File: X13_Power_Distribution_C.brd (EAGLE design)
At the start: 152.4 x 73.7 mm, 34 parts, among them Q1 IRF1018EPBF, Q2 310mA/60V/1.6Ω, Q3 IRF1018EPBF, Q4 IRF1018EPBF

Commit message: Version C! Uses connector C!
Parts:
- removed BRICK1, BRICK2: DIST2BRICK_B, Brick_Dist_Connector:DIST2BRICK_B
- added BRICK_A, BRICK_B: DIST2BRICK_C, Brick_Dist_Connector:DIST2BRICK_C
- moved R7 1.27 mm to (85.1, 24.1)
- moved R4 1.27 mm to (77.5, 24.1)
- moved R6 1.27 mm to (81.3, 24.1)
- moved R8 1.27 mm to (73.7, 24.1)
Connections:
- net +12V_A: now also BRICK_A.2@1, BRICK_A.2@10, BRICK_A.2@11, BRICK_A.2@12, BRICK_A.2@13, BRICK_A.2@14, BRICK_A.2@15, BRICK_A.2@16, BRICK_A.2@2, BRICK_A.2@3, BRICK_A.2@4, BRICK_A.2@5, BRICK_A.2@6, BRICK_A.2@7, BRICK_A.2@8, BRICK_A.2@9; no longer BRICK1.2@1, BRICK1.2@10, BRICK1.2@11, BRICK1.2@12, BRICK1.2@13, BRICK1.2@14, BRICK1.2@15, BRICK1.2@16, BRICK1.2@2, BRICK1.2@3, BRICK1.2@4, BRICK1.2@5, BRICK1.2@6, BRICK1.2@7, BRICK1.2@8, BRICK1.2@9
- net +12V_B: now also BRICK_B.2@1, BRICK_B.2@10, BRICK_B.2@11, BRICK_B.2@12, BRICK_B.2@13, BRICK_B.2@14, BRICK_B.2@15, BRICK_B.2@16, BRICK_B.2@2, BRICK_B.2@3, BRICK_B.2@4, BRICK_B.2@5, BRICK_B.2@6, BRICK_B.2@7, BRICK_B.2@8, BRICK_B.2@9; no longer BRICK2.2@1, BRICK2.2@10, BRICK2.2@11, BRICK2.2@12, BRICK2.2@13, BRICK2.2@14, BRICK2.2@15, BRICK2.2@16, BRICK2.2@2, BRICK2.2@3, BRICK2.2@4, BRICK2.2@5, BRICK2.2@6, BRICK2.2@7, BRICK2.2@8, BRICK2.2@9
- net +48V: now also BRICK_A.1@1, BRICK_A.1@10, BRICK_A.1@2, BRICK_A.1@3, BRICK_A.1@4, BRICK_A.1@5, BRICK_A.1@6, BRICK_A.1@7, BRICK_A.1@8, BRICK_A.1@9, BRICK_B.1@1, BRICK_B.1@10, BRICK_B.1@2, BRICK_B.1@3, BRICK_B.1@4, BRICK_B.1@5, BRICK_B.1@6, BRICK_B.1@7, BRICK_B.1@8, BRICK_B.1@9; no longer BRICK1.1@1, BRICK1.1@10, BRICK1.1@2, BRICK1.1@3, BRICK1.1@4, BRICK1.1@5, BRICK1.1@6, BRICK1.1@7, BRICK1.1@8, BRICK1.1@9, BRICK2.1@1, BRICK2.1@10, BRICK2.1@2, BRICK2.1@3, BRICK2.1@4, BRICK2.1@5, BRICK2.1@6, BRICK2.1@7, BRICK2.1@8, BRICK2.1@9
- net 12V_GND: now also BRICK_A.4@1, BRICK_A.4@10, BRICK_A.4@11, BRICK_A.4@12, BRICK_A.4@13, BRICK_A.4@14, BRICK_A.4@15, BRICK_A.4@16, BRICK_A.4@2, BRICK_A.4@3, BRICK_A.4@4, BRICK_A.4@5, BRICK_A.4@6, BRICK_A.4@7, BRICK_A.4@8, BRICK_A.4@9, BRICK_B.4@1, BRICK_B.4@10, BRICK_B.4@11, BRICK_B.4@12, BRICK_B.4@13, BRICK_B.4@14, BRICK_B.4@15, BRICK_B.4@16, BRICK_B.4@2, BRICK_B.4@3, BRICK_B.4@4, BRICK_B.4@5, BRICK_B.4@6, BRICK_B.4@7, BRICK_B.4@8, BRICK_B.4@9; no longer BRICK1.4@1, BRICK1.4@10, BRICK1.4@11, BRICK1.4@12, BRICK1.4@13, BRICK1.4@14, BRICK1.4@15, BRICK1.4@16, BRICK1.4@2, BRICK1.4@3, BRICK1.4@4, BRICK1.4@5, BRICK1.4@6, BRICK1.4@7, BRICK1.4@8, BRICK1.4@9, BRICK2.4@1, BRICK2.4@10, BRICK2.4@11, BRICK2.4@12, BRICK2.4@13, BRICK2.4@14, BRICK2.4@15, BRICK2.4@16, BRICK2.4@2, BRICK2.4@3, BRICK2.4@4, BRICK2.4@5, BRICK2.4@6, BRICK2.4@7, BRICK2.4@8, BRICK2.4@9
- net 48V_GND: now also BRICK_A.3@1, BRICK_A.3@10, BRICK_A.3@2, BRICK_A.3@3, BRICK_A.3@4, BRICK_A.3@5, BRICK_A.3@6, BRICK_A.3@7, BRICK_A.3@8, BRICK_A.3@9, BRICK_B.3@1, BRICK_B.3@10, BRICK_B.3@2, BRICK_B.3@3, BRICK_B.3@4, BRICK_B.3@5, BRICK_B.3@6, BRICK_B.3@7, BRICK_B.3@8, BRICK_B.3@9; no longer BRICK1.3@1, BRICK1.3@10, BRICK1.3@2, BRICK1.3@3, BRICK1.3@4, BRICK1.3@5, BRICK1.3@6, BRICK1.3@7, BRICK1.3@8, BRICK1.3@9, BRICK2.3@1, BRICK2.3@10, BRICK2.3@2, BRICK2.3@3, BRICK2.3@4, BRICK2.3@5, BRICK2.3@6, BRICK2.3@7, BRICK2.3@8, BRICK2.3@9
- net ALERT_1: now also BRICK_A.D; no longer BRICK1.D
- net ALERT_2: now also BRICK_B.D; no longer BRICK2.D
- net C2_1: now also BRICK_A.A; no longer BRICK1.A
- net C2_2: now also BRICK_B.A; no longer BRICK2.A
- net CLK: now also BRICK_A.C, BRICK_B.C; no longer BRICK1.C, BRICK2.C
- net DATA: now also BRICK_A.E, BRICK_B.E; no longer BRICK1.E, BRICK2.E
- net ON/OFF: now also BRICK_A.B, BRICK_B.B; no longer BRICK1.B, BRICK2.B
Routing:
- net +3.3V: track 142.4 -> 154.4 mm
- net ALERT_2: track 78.5 -> 70.5 mm
- net C2_1: track 66.0 -> 70.9 mm
- net CLK: track 89.6 -> 86.2 mm
- net C2_2: track 89.5 -> 86.4 mm, vias 2 -> 3
- net DATA: track 80.6 -> 79.2 mm
- net ON/OFF: track 79.4 -> 78.6 mm
- net ALERT_1: track 77.4 -> 76.9 mm

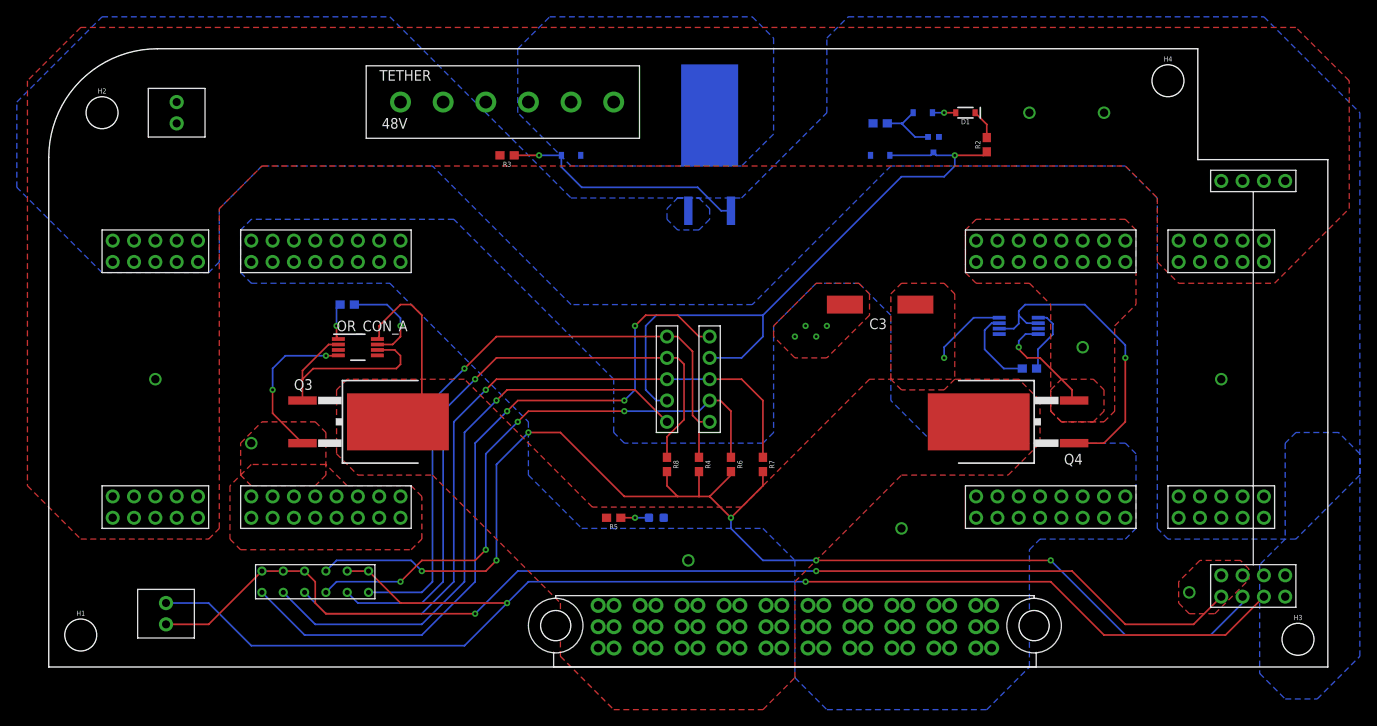
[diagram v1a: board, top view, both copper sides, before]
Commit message: 5V and 3.3V traces are wider now
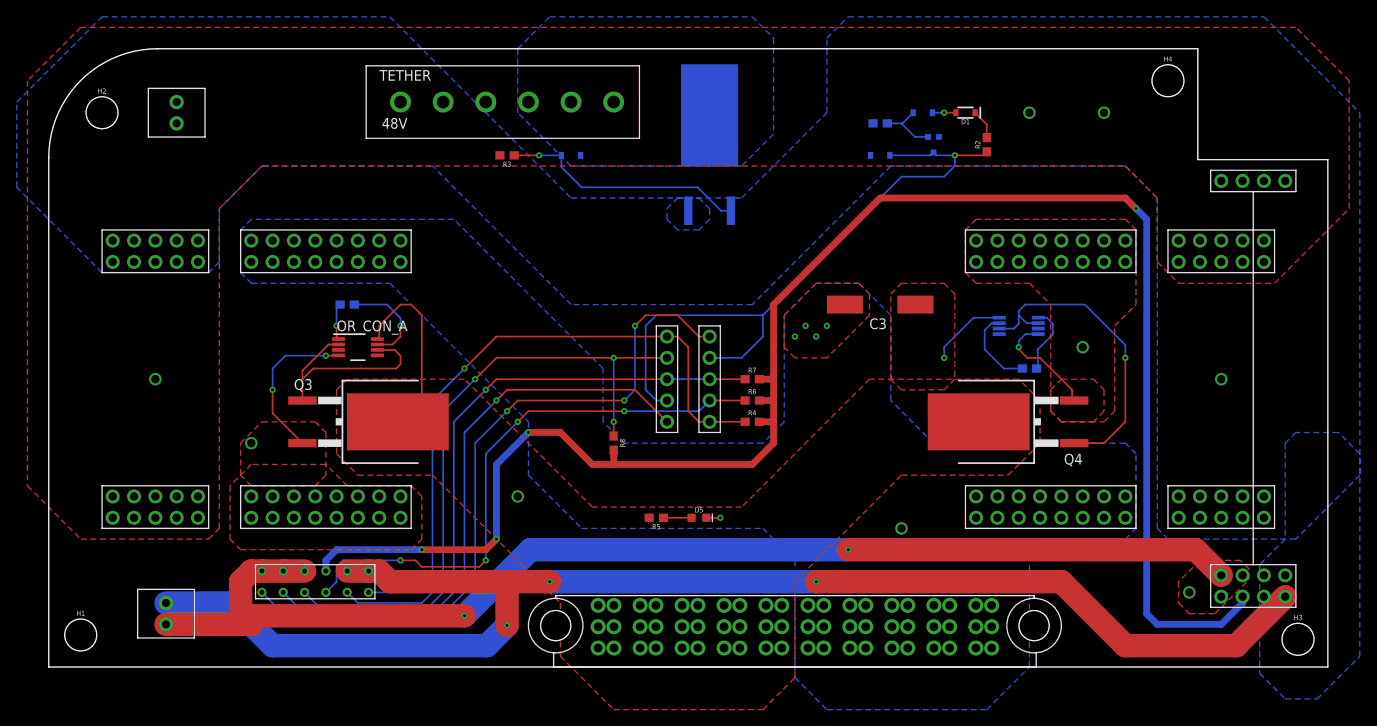
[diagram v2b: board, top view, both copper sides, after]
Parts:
- moved R7 10.2 mm to (83.8, 34.3), turned to 0 degrees
- moved R4 8.13 mm to (83.8, 29.2), turned to 0 degrees
- moved R6 8.03 mm to (83.8, 31.8), turned to 0 degrees
- moved R8 6.84 mm to (67.3, 26.7)
- moved D5 5.08 mm to (77.5, 17.8), flipped to the top, turned to 0 degrees
- moved R5 5.08 mm to (72.4, 17.8)
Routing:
- net +3.3V: track 154.4 -> 203.6 mm, vias 6 -> 4
- net CLK: track 86.2 -> 75.9 mm
- net +5V: track 138.1 -> 145.0 mm
- net 5V_GND: track 161.2 -> 166.8 mm, vias 2 -> 3
- net ALERT_1: track 76.9 -> 71.9 mm, vias 1 -> 3
- net ALERT_2: track 70.5 -> 68.5 mm
- net 12V_GND: track 0.00 -> 1.66 mm, vias 6 -> 7
- net C2_2: track 86.4 -> 85.2 mm
- net C2_1: track 70.9 -> 70.0 mm
- net N$8: vias 1 -> 0

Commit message: Moved ON/OFF, moved a diode
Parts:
- moved D2 10.2 mm to (109.2, 59.7), turned to 90 degrees
- moved D1 9.16 mm to (116.8, 61.0)
- moved D6 7.18 mm to (67.3, 55.9), turned to 270 degrees
- moved R1 6.35 mm to (99.1, 58.4)
- moved D3 4.58 mm to (106.7, 62.2)
- moved Q2 2.84 mm to (104.1, 59.7), turned to 90 degrees
- moved R2 2.84 mm to (113.0, 59.7)
- moved R3 2.54 mm to (54.6, 58.4)
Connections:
- net 48V_GND: now also D6.A
- net GND_RAW: no longer D6.A
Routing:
- net +3.3V: track 203.6 -> 195.2 mm
- net N$1: track 2.78 -> 8.39 mm
- net ON/OFF_DRIVE: track 7.44 -> 3.56 mm
- net ON/OFF: track 78.6 -> 80.1 mm

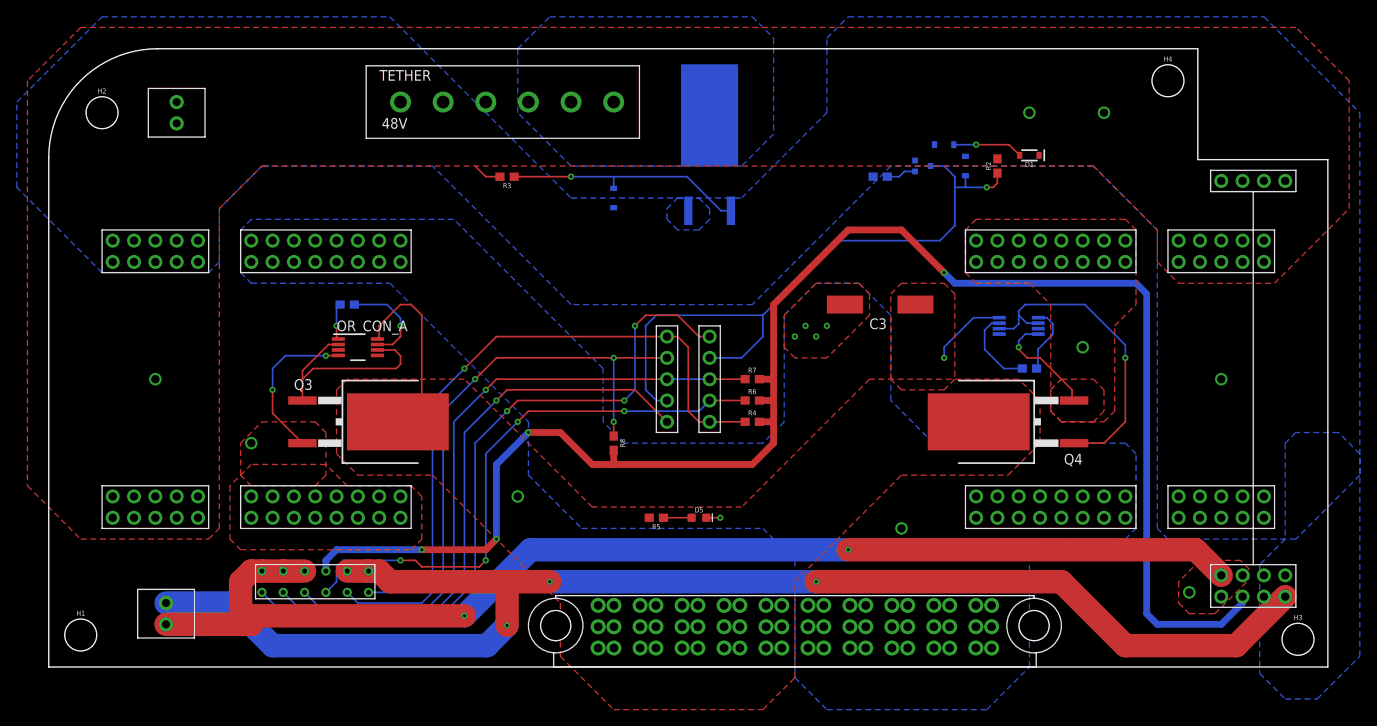
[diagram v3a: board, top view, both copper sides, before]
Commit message: Two LEDs where once was one
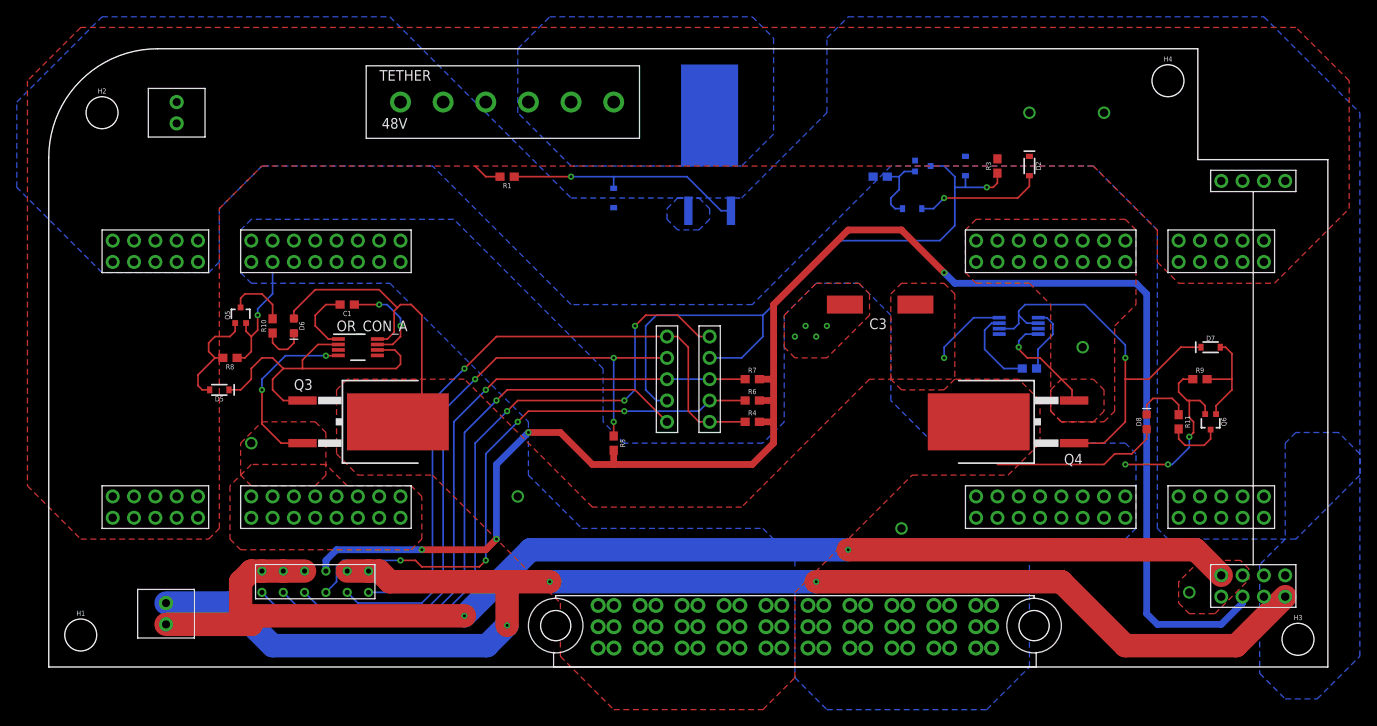
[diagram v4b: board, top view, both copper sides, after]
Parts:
- added D4: 5V, SparkFun-DiscreteSemi:SOD-323
- added D7: 15V, SparkFun-DiscreteSemi:SOD-323
- added D8: (no value), SparkFun-LED:LED-0603
- added Q5, Q6: SSM3K341R, SparkFun-DiscreteSemi:SOT323
- added R10, R11: 470, SparkFun-Resistors:0603
- added R9: 1M, SparkFun-Resistors:0603
- D1: value 22V -> 15V
- D2: value 5V -> 22V
- D5: value (none) -> 15V; device SparkFun-LED:LED-0603 -> SparkFun-DiscreteSemi:SOD-323
- D6: value 15V -> (none); device SparkFun-DiscreteSemi:SOD-323 -> SparkFun-LED:LED-0603
- Q2: value 310mA/60V/1.6Ω -> SSM3K341R
- R2, R8: value 10k -> 1M
- R3: value 1M -> 10k
- R5: value 470 -> 10k
- moved D5 59.1 mm to (20.3, 33.0), turned to 180 degrees
- moved R3 58.4 mm to (113.0, 59.7), turned to 90 degrees
- moved D1 49.8 mm to (67.3, 55.9), flipped to the bottom, turned to 270 degrees
- moved R8 46.8 mm to (21.6, 36.8), turned to 180 degrees
- moved R1 44.5 mm to (54.6, 58.4), flipped to the top
- moved D6 41.0 mm to (29.2, 40.6), flipped to the top
- moved R2 14.0 mm to (99.1, 58.4), flipped to the bottom, turned to 180 degrees
- moved R5 10.2 mm to (67.3, 26.7), turned to 270 degrees
- moved D3 8.52 mm to (102.9, 54.6)
- moved D2 7.62 mm to (116.8, 59.7), flipped to the top, turned to 270 degrees
- flipped C1 to the top, turned to 180 degrees
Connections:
- removed net N$8: D5.A, R5.1
- new net LED_DRIVE_A: D5.A, Q5.1, R8.2
- new net LED_DRIVE_B: D7.A, Q6.1, R9.2
- new net N$4: Q5.3, R10.2
- new net N$5: D6.C, R10.1
- new net N$6: Q6.3, R11.2
- new net N$7: D8.C, R11.1
- net +12V: now also D6.A, D8.A; no longer R5.2
- net +3.3V: now also R5.2; no longer R8.2
- net +48V: now also D2.C, R1.2; no longer D1.C, R2.2
- net 12V_GND: now also Q5.2, Q6.2, R8.1, R9.1; no longer D5.C
- net 48V_GND: now also D1.A, D4.A, R2.1; no longer D2.A, D6.A, R1.1
- net ALERT_1: now also R5.1; no longer R8.1
- net N$1: now also D2.A; no longer D1.A
- net ON/OFF: now also D4.C, R3.1; no longer D2.C, R2.1
- net ON/OFF_DRIVE: now also R2.2; no longer R1.2
- net OR_DRIVE_A: now also D5.C
- net OR_DRIVE_B: now also D7.C
- net REV_DRIVE: now also D1.C, R1.1; no longer D6.C, R3.1
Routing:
- net +12V: track 33.0 -> 69.1 mm
- net 12V_GND: track 1.66 -> 36.5 mm, vias 7 -> 9
- net OR_DRIVE_A: track 25.6 -> 40.8 mm
- net LED_DRIVE_A: track 0.00 -> 13.5 mm
- net LED_DRIVE_B: track 0.00 -> 12.7 mm
- net OR_DRIVE_B: track 38.1 -> 48.7 mm
- net N$4: track 0.00 -> 7.34 mm
- net N$1: track 8.39 -> 15.2 mm
- net N$7: track 0.00 -> 6.78 mm
- net N$6: track 0.00 -> 6.73 mm
- net N$5: track 0.00 -> 5.51 mm
- net ON/OFF_DRIVE: track 3.56 -> 8.88 mm
- net VCAPL_A: track 4.35 -> 8.16 mm, vias 1 -> 0
- net N$8: track 3.35 -> 0.00 mm
- net +12V_A: track 18.8 -> 21.4 mm
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
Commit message: Some tweaks and labeling
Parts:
- R10: value 470 -> 1M
- R9: value 1M -> 470
- moved R10 110.7 mm to (137.2, 34.3), turned to 0 degrees
- moved R9 110.7 mm to (26.7, 40.6), turned to 90 degrees
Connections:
- net 12V_GND: now also R10.1; no longer R9.1
- net LED_DRIVE_B: now also R10.2; no longer R9.2
- net N$4: now also R9.2; no longer R10.2
- net N$5: now also R9.1; no longer R10.1
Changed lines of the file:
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@@
 <attribute name="VALUE" x="21.59" y="37.592" size="0.6096" layer="27" font="vector" ratio="20" rot="R180" align="top-center"/>
 </element>
-<element name="R10" library="SparkFun-Resistors" library_urn="urn:adsk.eagle:library:532" package="0603" package3d_urn="urn:adsk.eagle:package:39650/1" value="470" x="26.67" y="40.64" smashed="yes" rot="R90">
+<element name="R9" library="SparkFun-Resistors" library_urn="urn:adsk.eagle:library:532" package="0603" package3d_urn="urn:adsk.eagle:package:39650/1" value="470" x="26.67" y="40.64" smashed="yes" rot="R90">
 <attribute name="NAME" x="25.908" y="40.64" size="0.6096" layer="25" font="vector" ratio="20" rot="R90" align="bottom-center"/>
 <attribute name="PROD_ID" value=" " x="26.67" y="40.64" size="1.778" layer="27" rot="R90" display="off"/>
@@
 <attribute name="VALUE" x="138.43" y="37.338" size="0.6096" layer="27" font="vector" ratio="20" align="top-center"/>
 </element>
-<element name="R9" library="SparkFun-Resistors" library_urn="urn:adsk.eagle:library:532" package="0603" package3d_urn="urn:adsk.eagle:package:39650/1" value="1M" x="137.16" y="34.29" smashed="yes">
+<element name="R10" library="SparkFun-Resistors" library_urn="urn:adsk.eagle:library:532" package="0603" package3d_urn="urn:adsk.eagle:package:39650/1" value="1M" x="137.16" y="34.29" smashed="yes">
 <attribute name="NAME" x="137.16" y="35.052" size="0.6096" layer="25" font="vector" ratio="20" align="bottom-center"/>
 <attribute name="PROD_ID" value=" " x="138.43" y="30.48" size="1.778" layer="27" display="off"/>
@@
 <contactref element="R8" pad="1"/>
 <contactref element="Q5" pad="2"/>
-<contactref element="R9" pad="1"/>
+<contactref element="R10" pad="1"/>
 <contactref element="Q6" pad="2"/>
 <wire x1="23.51" y1="40.985" x2="23.51" y2="39.99" width="0.2032" layer="1"/>
@@
 <signal name="N$4">
 <contactref element="Q5" pad="3"/>
-<contactref element="R10" pad="2"/>
+<contactref element="R9" pad="2"/>
 <wire x1="22.86" y1="43.942" x2="23.368" y2="44.45" width="0.2032" layer="1"/>
 <wire x1="23.368" y1="44.45" x2="25.4" y2="44.45" width="0.2032" layer="1"/>
@@
 </signal>
 <signal name="N$5">
-<contactref element="R10" pad="1"/>
+<contactref element="R9" pad="1"/>
 <contactref element="D6" pad="C"/>
 <wire x1="29.21" y1="39.763" x2="29.21" y2="38.608" width="0.2032" layer="1"/>
@@
 </signal>
 <signal name="LED_DRIVE_B">
-<contactref element="R9" pad="2"/>
+<contactref element="R10" pad="2"/>
 <contactref element="D7" pad="A"/>
 <contactref element="Q6" pad="1"/>

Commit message: Moved 5V Ethernet, added some cutouts
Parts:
- moved 5V_POE 113.1 mm to (127.0, 10.2), turned to 180 degrees
- moved D5 1.27 mm to (21.6, 33.0)
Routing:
- net 5V_GND: track 166.8 -> 119.9 mm, vias 3 -> 2
- net +5V: track 145.0 -> 152.0 mm, vias 3 -> 2
- net OR_DRIVE_A: track 40.8 -> 35.4 mm
- removed copper zone on layer 1, net +5V

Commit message: Jan 2nd Tweaks
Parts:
- moved C3 35.1 mm to (76.2, 16.5), turned to 90 degrees
- moved TETHER 15.5 mm to (26.7, 64.8)
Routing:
- net +12V: track 69.1 -> 76.0 mm
